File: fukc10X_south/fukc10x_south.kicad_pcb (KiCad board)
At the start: 2 copper layers, 427.1 x 120.2 mm, 276 parts, among them J1 SM04B-SRSS-TB, J2 LED_Conn01x02_Pin, J3 LED_Conn01x02_Pin, J4 LED_Conn01x02_Pin, J5 LED_Conn01x02_Pin, J6 LED_Conn01x02_Pin, J7 LED_Conn01x02_Pin, J8 LED_Conn01x02_Pin, U1 XC6206P332MR, U2 STM32F072CBT6

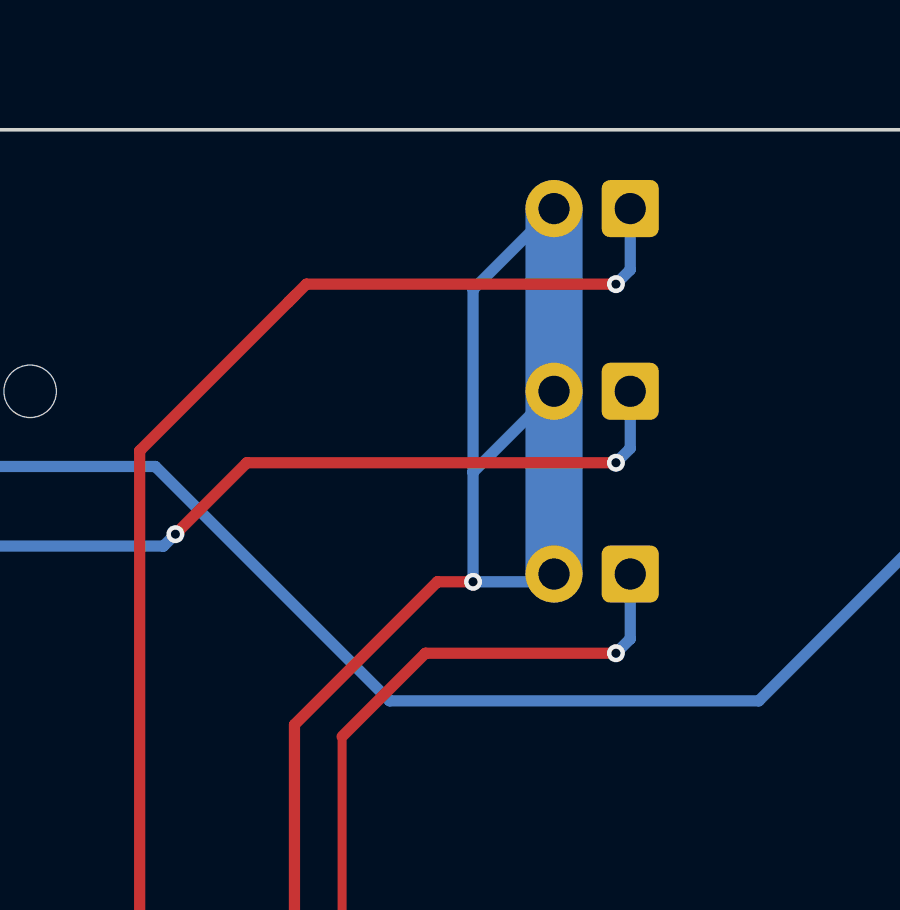
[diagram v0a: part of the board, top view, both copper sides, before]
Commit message: moved forgotten leds
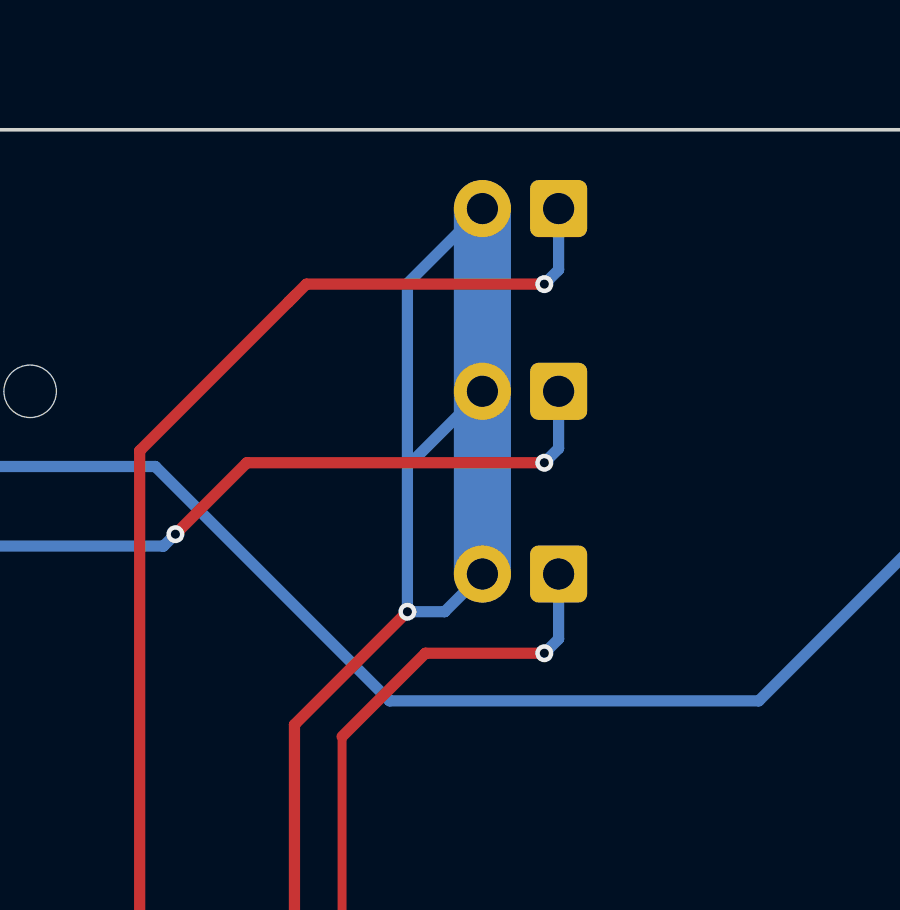
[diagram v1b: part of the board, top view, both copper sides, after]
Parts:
- moved J6 2.39 mm to (453.2, 97.4)
- moved J7 2.39 mm to (453.2, 103.5)
- moved J8 2.39 mm to (453.2, 109.6)
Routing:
- net LedCaps: track 519.5 -> 517.2 mm
- net LedScroll: track 118.0 -> 115.6 mm
- net LedNum: track 115.0 -> 112.6 mm
- net +5V: track 612.2 -> 610.5 mm
